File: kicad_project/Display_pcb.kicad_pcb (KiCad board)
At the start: 4 copper layers, 60.6 x 27.6 mm, 89 parts, among them IC1 ESP32-S3R8, J1 Micro_SD_Card_Det_Hirose_DM3AT, J2 USB C, J8 33FXRH-SM1-GAN-TF, Q1 S8050, Q2 BSS84, Q3 S8050, SW1 B3U-1000P, SW2 B3U-1000P, SW3 B3U-1000P, U1 W25Q128JVSIQ, U2 SY8089A1AAC, U3 AXPM65611, U5 USBLC6-2SC6, Y1 40MHz

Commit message: Pcb to production
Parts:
- removed D2: B5819W, Diode_SMD:D_SOD-123
- removed L7, L8: DFP252012TF-100M, smd-non-ipc:DFE252012P-1R0M=P2
- removed Q1, Q3: S8050, Package_TO_SOT_SMD:SOT-23
- removed Q2: BSS84, Package_TO_SOT_SMD:SOT-23
- removed R22: TBD, Resistor_SMD:R_0402_1005Metric
- removed R30: 100k, Resistor_SMD:R_0402_1005Metric
- removed R31: 680k, Resistor_SMD:R_0402_1005Metric
- removed TP6: VDD_SPI, TestPoint:TestPoint_Pad_D1.0mm
- removed TP7: +5V, TestPoint:TestPoint_Pad_D1.0mm
- added C34: 22uF, Capacitor_SMD:C_0402_1005Metric, F.Cu at (144.6, 92.1)
- added C35: 100nF, Capacitor_SMD:C_0402_1005Metric, F.Cu at (143.8, 92.1)
- added C36: 22uF, Capacitor_SMD:C_0402_1005Metric, F.Cu at (143.0, 92.1)
- added C37: 22uF, Capacitor_SMD:C_0402_1005Metric, F.Cu at (152.8, 95.4)
- added D1: SS34, Diode_SMD:D_SMA, F.Cu at (151.8, 88.8)
- added DS3: GREEN, LED_SMD:LED_0603_1608Metric, F.Cu at (142.7, 88.4)
- added G***: LOGO, logo:OSHWA_Certification.kicad_sym, B.Cu at (169.8, 106.8)
- added L4: 1uH, smd-non-ipc:BR2518_YDN, F.Cu at (146.6, 89.2)
- added L6: 22uH, smd-non-ipc:MDA7030-220M, F.Cu at (159.4, 92.4)
- added NT1: NetTie_2, NetTie:NetTie-2_SMD_Pad0.5mm, F.Cu at (158.2, 101.3)
- added NT2: NetTie_2, NetTie:NetTie-2_SMD_Pad0.5mm, F.Cu at (156.7, 101.3)
- added R17: 22k, Resistor_SMD:R_0402_1005Metric, F.Cu at (148.5, 93.8)
- added R18: 0R, Resistor_SMD:R_0402_1005Metric, F.Cu at (143.4, 90.6)
- added R23: 1k, Resistor_SMD:R_0603_1608Metric_Pad0.98x0.95mm_HandSolder, F.Cu at (144.1, 88.5)
- added U4: SY8089A1AAC, smd-non-ipc:SOT95P285X130-5N, F.Cu at (146.6, 93.0)
- C18, C30: value 10uF -> 22uF
- C27: value 10uF -> 22uF; moved to F.Cu
- C28: value 1uF -> 22uF; footprint Capacitor_SMD:C_0603_1608Metric -> Capacitor_SMD:C_0402_1005Metric
- C29: value 1uF -> 100nF; footprint Capacitor_SMD:C_0603_1608Metric -> Capacitor_SMD:C_0402_1005Metric
- C31: value 10uF -> 6.8pF; moved to F.Cu
- C32, C33: moved to F.Cu
- G***, R1, R2, R8: moved to B.Cu
- J2: footprint hwlab:USB_C_Receptacle_HCTL_HC019-1E1H1A103-0HR -> paltatech:USB_C_Receptacle_HCTL_HC019-1E1H1A103-0HR
- R10: value 22k -> 10k
- R13: value 0R -> 100k
- R14: value 0R -> 100k; moved to F.Cu
- R20: value 0R -> 10k
- R21: value 0R -> 80k6
- R7: value 100k -> 10k
- R9: value 100k -> 64k9
- SW1, SW2, SW3: footprint hwlab:B3U-1000P -> smd-non-ipc:B3U-1000P
- TP2: value +3V3 -> +4V6
- TP3: value +4V6 -> +5V4
- TP4: value -2V2 -> +3V3
- U3: value AXPM65611 -> MT3608; footprint smd-non-ipc:DFN-12 -> Package_TO_SOT_SMD:SOT-23-6
- moved G*** 220.4 mm to (173.8, 110.0), turned to 90 degrees
- moved C32 177.2 mm to (158.2, 103.5), turned to -90 degrees
- moved C33 176.8 mm to (156.7, 103.5), turned to -90 degrees
- moved TP1 175.9 mm to (149.6, 96.5)
- moved C27 175.6 mm to (152.8, 97.0)
- moved DS1 173.1 mm to (127.5, 105.7)
- moved U3 172.6 mm to (153.3, 92.8), turned to -90 degrees
- moved C14 171.6 mm to (139.2, 106.5)
- moved C18 171.5 mm to (150.7, 91.3), turned to -90 degrees
- moved C23 171.5 mm to (137.9, 92.0), turned to -90 degrees
- moved C24 171.5 mm to (137.1, 92.0), turned to -90 degrees
- moved R11 171.4 mm to (139.7, 96.0), turned to -90 degrees
- moved C22 171.4 mm to (138.8, 92.0), turned to -90 degrees
- moved R32 171.2 mm to (137.5, 90.5), turned to 0 degrees
- moved C15 171.1 mm to (134.3, 106.3), turned to 180 degrees
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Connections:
- C18 pad 1: Net-(Q3-C) -> Net-(D1-K)
- C27 pad 1: EAVDD -> /POWER/VBUS
- C28 pad 1: +3V3 -> /POWER/VBUS
- C29 pad 1: +3V3 -> VCC
- C30 pad 1: -2V2 -> VCC
- C31 pad 1: 4.6V -> Net-(C31-Pad1)
- C31 pad 2: GND -> Net-(U4-FB)
- C32 pad 1: +3V3 -> /AVDD
- C33 pad 1: +3V3 -> Net-(J8-Pin_26)
- IC1 pad 38: unconnected-(IC1-GPIO33-Pad38) -> /MCU/GPIO33
- IC1 pad 43: /OL_EN -> /GPIO38
- J2 pad A4: VBUS -> /POWER/VBUS
- J2 pad A9: VBUS -> /POWER/VBUS
- J2 pad B4: VBUS -> /POWER/VBUS
- J2 pad B9: VBUS -> /POWER/VBUS
- J8 pad 1: unconnected-(J8-Pin_1-Pad1) -> GND
- J8 pad 10: /OL_EN -> unconnected-(J8-Pin_10-Pad10)
- J8 pad 11: /OL_TE -> unconnected-(J8-Pin_11-Pad11)
- J8 pad 12: /OL_RESET -> unconnected-(J8-Pin_12-Pad12)
- J8 pad 13: /OL_SD0 -> unconnected-(J8-Pin_13-Pad13)
- J8 pad 14: /OL_D0 -> unconnected-(J8-Pin_14-Pad14)
- J8 pad 15: /OL_D1 -> /OL_D3
- J8 pad 16: /OL_SCK -> /OL_D2
- J8 pad 18: /OL_D2 -> /OL_SCK
- J8 pad 19: /OL_D3 -> /OL_D1
- J8 pad 2: unconnected-(J8-Pin_2-Pad2) -> GND
- J8 pad 20: unconnected-(J8-Pin_20-Pad20) -> /OL_D0
- J8 pad 21: unconnected-(J8-Pin_21-Pad21) -> /OL_SD0
- J8 pad 22: unconnected-(J8-Pin_22-Pad22) -> /OL_RESET
- J8 pad 23: unconnected-(J8-Pin_23-Pad23) -> /OL_TE
- J8 pad 26: /IM1 -> Net-(J8-Pin_26)
- J8 pad 27: /IM0 -> /AVDD
- J8 pad 3: unconnected-(J8-Pin_3-Pad3) -> 4.6V
- J8 pad 30: 4.6V -> unconnected-(J8-Pin_30-Pad30)
- J8 pad 31: 4.6V -> unconnected-(J8-Pin_31-Pad31)
- J8 pad 32: -2V2 -> unconnected-(J8-Pin_32-Pad32)
- J8 pad 33: -2V2 -> unconnected-(J8-Pin_33-Pad33)
- J8 pad 4: unconnected-(J8-Pin_4-Pad4) -> 4.6V
- J8 pad 7: EAVDD -> GND
- J8 pad 9: /SWIRE -> unconnected-(J8-Pin_9-Pad9)
- R11 pad 2: VCC -> /MCU/GPIO1
- R13 pad 1: Net-(U3-CTRL) -> Net-(U4-EN)
- R13 pad 2: /SWIRE -> VCC
- R14 pad 1: Net-(U3-EN) -> Net-(C31-Pad1)
- R14 pad 2: /OL_EN -> Net-(U4-FB)
- R16 pad 2: +3V3 -> 4.6V
- R19 pad 1: /IM1 -> Net-(D1-K)
- R19 pad 2: +3V3 -> VCC
- R20 pad 1: /IM0 -> Net-(U3-FB)
- R20 pad 2: +3V3 -> GND
- R21 pad 1: GND -> Net-(D1-K)
- R21 pad 2: /IM0 -> Net-(U3-FB)
- R32 pad 2: +3V3 -> 4.6V
- R7 pad 1: VBUS -> +3V3
- R7 pad 2: Net-(Q1-C) -> /MCU/GPIO33
- SW3 pad 1: Net-(Q1-B) -> GND
- SW3 pad 2: Net-(Q3-C) -> /MCU/GPIO33
- TP1 pad 1: VBUS -> /POWER/VBUS
- TP3 pad 1: 4.6V -> Net-(D1-K)
- TP4 pad 1: -2V2 -> Net-(C31-Pad1)
- U3 pad 3: 4.6V -> Net-(U3-FB)
- U3 pad 4: Net-(U3-EN) -> /POWER/VBUS
- U3 pad 5: GND -> /POWER/VBUS
- U5 pad 5: VBUS -> /POWER/VBUS
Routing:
- net /OL_EN: track 51.9 -> 0.00 mm, vias 5 -> 0
- net /POWER/VBUS: track 0.00 -> 47.9 mm, vias 0 -> 5
- net VBUS: track 38.0 -> 0.00 mm, vias 6 -> 0
- net /MCU/GPIO33: track 0.00 -> 36.6 mm, vias 0 -> 2
- net GND: track 104.2 -> 135.7 mm, vias 333 -> 291
- net Net-(D1-A): track 1.75 -> 31.7 mm
- net -2V2: track 29.0 -> 0.00 mm, vias 4 -> 0
- net Net-(C31-Pad1): track 0.00 -> 28.1 mm, vias 0 -> 2
- net Net-(Q3-C): track 22.2 -> 0.00 mm
- net Net-(Q1-B): track 20.5 -> 0.00 mm, vias 2 -> 0
- net Net-(D1-K): track 0.00 -> 20.3 mm
- net /SWIRE: track 16.1 -> 0.00 mm, vias 1 -> 0
- net EAVDD: track 15.6 -> 0.00 mm, vias 1 -> 0
- net /MCU/GPIO1: track 4.61 -> 17.1 mm, vias 0 -> 2
- net +3V3: track 41.3 -> 29.0 mm, vias 11 -> 9
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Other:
- board text added: "BOOT"
- board text added: "DISPLAY"
- board text added: "RESET"

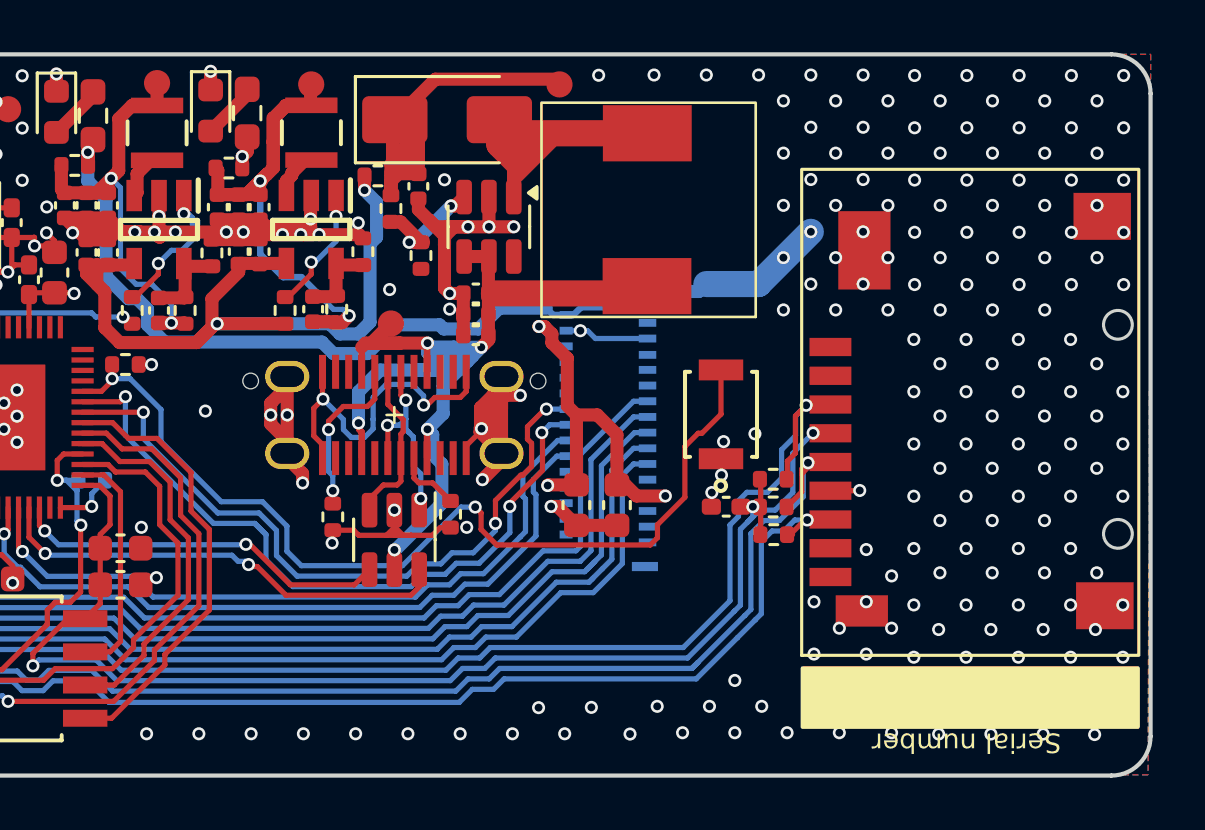
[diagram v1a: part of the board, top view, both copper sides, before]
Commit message: Remove USB preregulator from power circuit
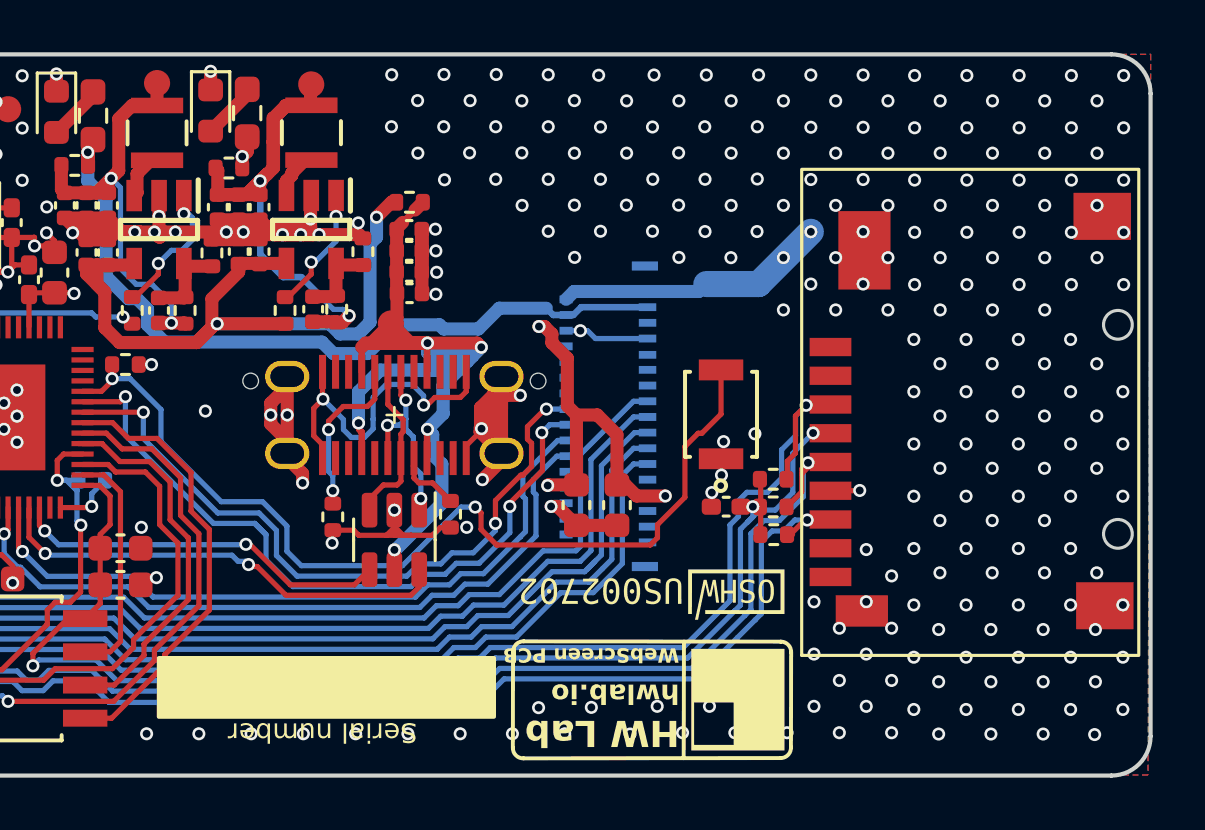
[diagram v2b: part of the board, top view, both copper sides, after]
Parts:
- removed D1: SS34, Diode_SMD:D_SMA
- removed L6: 22uH, smd-non-ipc:MDA7030-220M
- removed R20: 10k, Resistor_SMD:R_0402_1005Metric
- removed R21: 80k6, Resistor_SMD:R_0402_1005Metric
- removed TP3: +5V4, TestPoint:TestPoint_Pad_D1.0mm
- removed U3: MT3608, Package_TO_SOT_SMD:SOT-23-6
- G*** (x2): moved to F.Cu
- moved G*** 11.0 mm to (162.8, 110.9), turned to 180 degrees
- moved G*** 10.2 mm to (159.6, 106.9), turned to 180 degrees
- moved C27 4.77 mm to (150.3, 93.0), turned to 0 degrees
- moved C18 4.10 mm to (150.3, 95.4), turned to 0 degrees
- moved C28 3.52 mm to (150.3, 93.8), turned to 0 degrees
- moved C37 2.68 mm to (150.3, 94.6), turned to 0 degrees
- moved R19 1.58 mm to (150.3, 91.9)
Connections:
- C18 pad 1: Net-(D1-K) -> /POWER/VBUS
- R19 pad 1: Net-(D1-K) -> /POWER/VBUS
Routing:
- net Net-(D1-A): track 31.7 -> 0.00 mm
- net Net-(D1-K): track 20.3 -> 0.00 mm
- net GND: track 135.7 -> 127.3 mm, vias 291 -> 334
- net Net-(U3-FB): track 4.84 -> 0.00 mm, vias 2 -> 0
- net /POWER/VBUS: track 47.9 -> 51.4 mm
- net VCC: track 30.7 -> 29.9 mm
